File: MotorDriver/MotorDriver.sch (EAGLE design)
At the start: 52 parts, among them CN1 53375-0610, Q1 BUK7Y7R8-80EX, Q2 BUK7Y7R8-80EX, Q3 BUK7Y7R8-80EX, Q4 BUK7Y7R8-80EX, Q5 BUK7Y7R8-80EX, Q6 BUK7Y7R8-80EX, U1 LPC1549JBD48, U2 DRV8320SRTVT, U3 MCP1700T-33, U4 ADR5041

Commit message: SCT1_OUT[5, 6]を使うために配線を入れ替えた
1:    PWM_CL->MOSI
2:    PWM_CH->RX
22: RX->PWM_CH
33  MOSI->PWM_CL
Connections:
- net MOSI: now also U1.PIO0_0/ADC0_10/SCT0_OUT3; no longer U1.SWDIO/PIO0_20/SCT1_OUT6/TMS
- net PWM_CH: now also U1.PIO0_14/ADC1_7/SCT1_OUT5; no longer U1.PIO0_1/ADC0_7/SCT0_OUT4
- net PWM_CL: now also U1.SWDIO/PIO0_20/SCT1_OUT6/TMS; no longer U1.PIO0_0/ADC0_10/SCT0_OUT3
- net RX: now also U1.PIO0_1/ADC0_7/SCT0_OUT4; no longer U1.PIO0_14/ADC1_7/SCT1_OUT5
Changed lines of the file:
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@@
-</segment>
-</net>
-<net name="PWM_CH" class="0">
-<segment>
-<wire x1="10.16" y1="99.06" x2="-10.16" y2="99.06" width="0.1524" layer="91"/>
-<label x="-10.16" y="99.06" size="1.778" layer="95"/>
-<pinref part="U1" gate="G$1" pin="PIO0_1/ADC0_7/SCT0_OUT4"/>
-</segment>
-</net>
-<net name="PWM_CL" class="0">
-<segment>
-<wire x1="-10.16" y1="101.6" x2="10.16" y2="101.6" width="0.1524" layer="91"/>
-<label x="-10.16" y="101.6" size="1.778" layer="95"/>
-<pinref part="U1" gate="G$1" pin="PIO0_0/ADC0_10/SCT0_OUT3"/>
 </segment>
 </net>
@@
 <net name="RX" class="0">
 <segment>
-<pinref part="U1" gate="G$1" pin="PIO0_14/ADC1_7/SCT1_OUT5"/>
-<wire x1="60.96" y1="30.48" x2="60.96" y2="17.78" width="0.1524" layer="91"/>
-<label x="60.96" y="17.78" size="1.778" layer="95" rot="R90"/>
-</segment>
-<segment>
 <wire x1="203.2" y1="48.26" x2="187.96" y2="48.26" width="0.1524" layer="91"/>
 <label x="195.58" y="48.26" size="1.778" layer="95" rot="MR0"/>
 <pinref part="R27" gate="G$1" pin="1"/>
+</segment>
+<segment>
+<pinref part="U1" gate="G$1" pin="PIO0_1/ADC0_7/SCT0_OUT4"/>
+<wire x1="10.16" y1="99.06" x2="-10.16" y2="99.06" width="0.1524" layer="91"/>
+<label x="-10.16" y="99.06" size="1.778" layer="95"/>
 </segment>
 </net>
@@
 <net name="MOSI" class="0">
 <segment>
-<pinref part="U1" gate="G$1" pin="SWDIO/PIO0_20/SCT1_OUT6/TMS"/>
-<wire x1="93.98" y1="93.98" x2="109.22" y2="93.98" width="0.1524" layer="91"/>
-<label x="96.52" y="93.98" size="1.778" layer="95"/>
-</segment>
-<segment>
 <wire x1="137.16" y1="96.52" x2="124.46" y2="96.52" width="0.1524" layer="91"/>
 <label x="124.46" y="96.52" size="1.778" layer="95"/>
 <pinref part="CN1" gate="G$1" pin="4"/>
+</segment>
+<segment>
+<pinref part="U1" gate="G$1" pin="PIO0_0/ADC0_10/SCT0_OUT3"/>
+<wire x1="10.16" y1="101.6" x2="-10.16" y2="101.6" width="0.1524" layer="91"/>
+<label x="-10.16" y="101.6" size="1.778" layer="95"/>
 </segment>
 </net>
@@
 </segment>
 </net>
+<net name="PWM_CL" class="0">
+<segment>
+<pinref part="U1" gate="G$1" pin="SWDIO/PIO0_20/SCT1_OUT6/TMS"/>
+<wire x1="93.98" y1="93.98" x2="109.22" y2="93.98" width="0.1524" layer="91"/>
+<label x="96.52" y="93.98" size="1.778" layer="95"/>
+</segment>
+</net>
+<net name="PWM_CH" class="0">
+<segment>
+<pinref part="U1" gate="G$1" pin="PIO0_14/ADC1_7/SCT1_OUT5"/>
+<wire x1="60.96" y1="30.48" x2="60.96" y2="17.78" width="0.1524" layer="91"/>
+<label x="60.96" y="17.78" size="1.778" layer="95" rot="R90"/>
+</segment>
+</net>

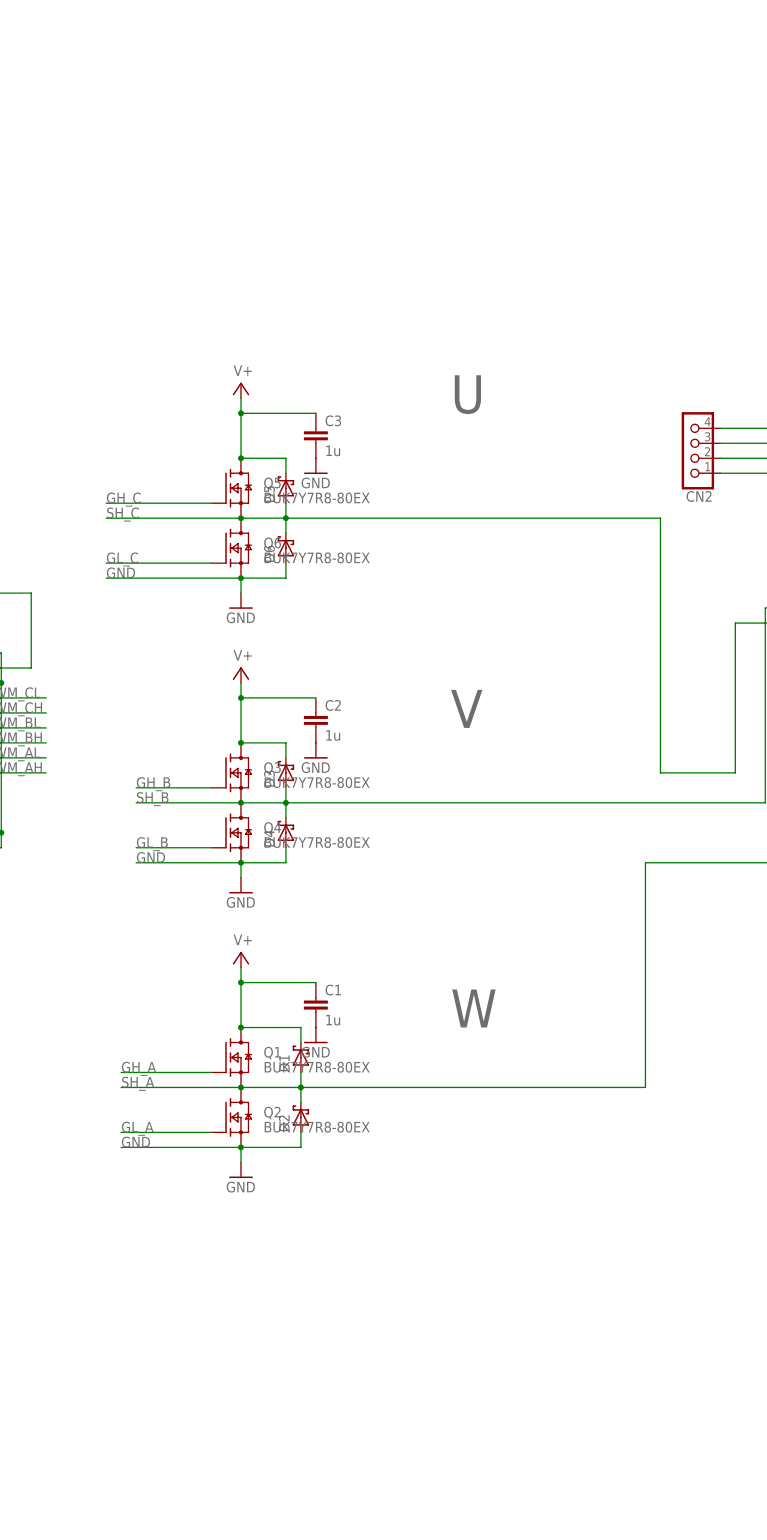
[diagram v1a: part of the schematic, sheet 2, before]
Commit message: FETのゲートソース間に抵抗を追加
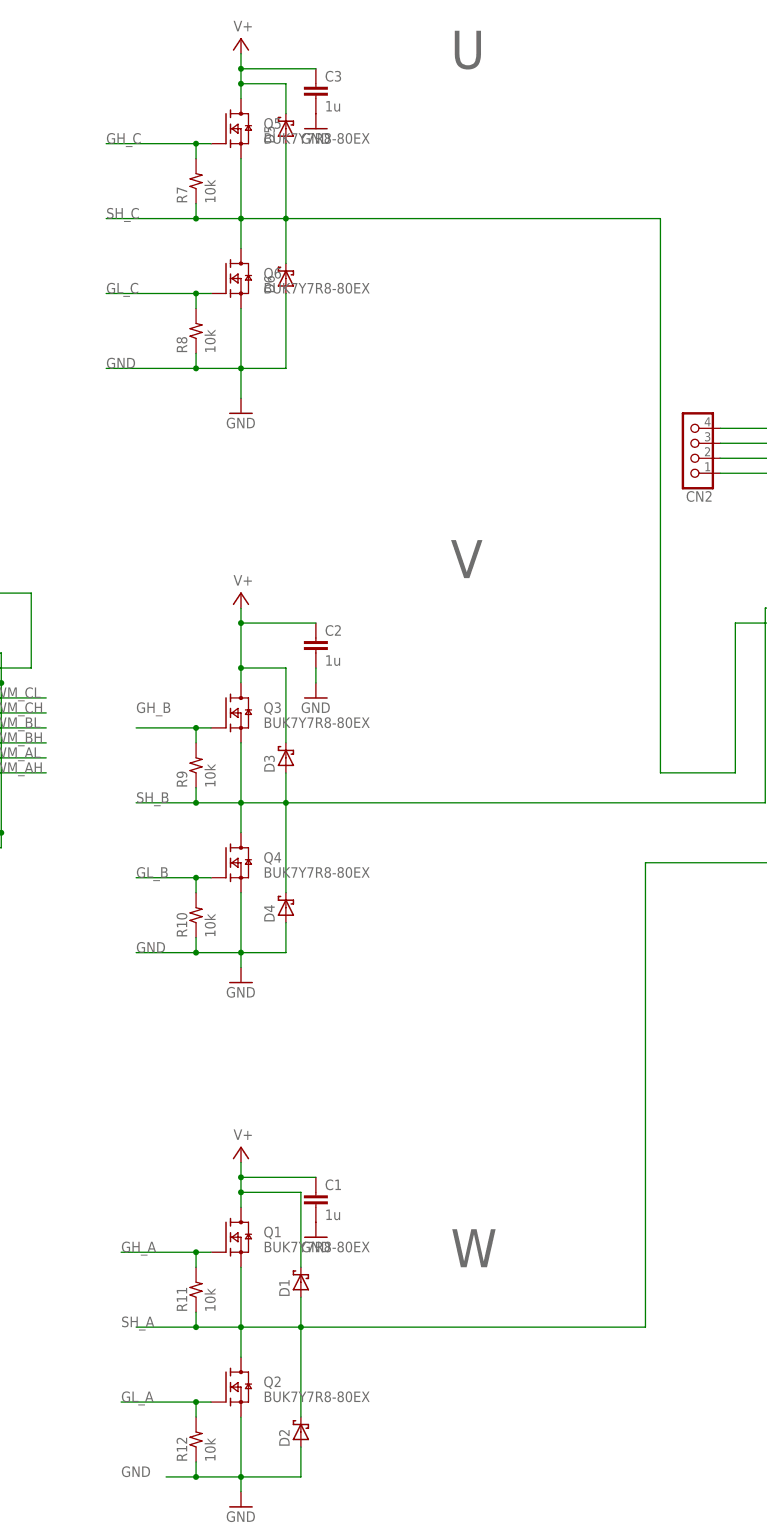
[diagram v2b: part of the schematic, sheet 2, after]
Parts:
- added R10, R11, R12, R7, R8, R9: 10k, Passive:R1608
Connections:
- net GH_A: now also R11.2
- net GH_B: now also R9.2
- net GH_C: now also R7.2
- net GL_A: now also R12.2
- net GL_B: now also R10.2
- net GL_C: now also R8.2
- net GND: now also R10.1, R12.1, R8.1
- net SH_A: now also R11.1
- net SH_B: now also R9.1
- net SH_C: now also R7.1
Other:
- moved on the sheet: C1, C2, C3, D1, D2, D3, D4, D5, D6, Q1, Q2, Q3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

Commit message: nya-n
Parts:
- C1, C10, C19, C2, C20, C3, C6, C9: device MotorDriver_Rev1:PASSIVE_C2012 -> MotorDriver:C2012
- C22, C23, C24: device Passive:C1608 -> MotorDriver:C1608
- C8: device MotorDriver_Rev1:PASSIVE_C1608 -> MotorDriver:C1608
- D7: device MotorDriver_Rev1:DIODE_SBD-SOD523 -> MotorDriver:SBD-SOD523
- LED0, LED1, LED2: device Opto:LED1608 -> MotorDriver:LED1608
- LED3: device Opto:LED1611R -> MotorDriver:LED1608
- R1, R10, R11, R12, R17, R2, R21, R23, R26, R27, R3, R32, R4, R5, R6, R7, R8, R9: device Passive:R1608 -> MotorDriver:R1608
- U1: device LPC1549JBD48:LPC1549JBD48 -> MotorDriver:LPC1549JBD48
- U2: device DRV8320SRTVT:DRV8320SRTVT -> MotorDriver:DRV8320SRTVT

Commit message: 機能追加 *CANバス *ホールセンサをダイレクトでDRVへ入力 *電源電圧監視 *DCDCをGDに内蔵 *15Aヒューズ
機能削減
*UART-DFUを廃止
*SPI接続を廃止
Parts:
- removed CN1: 53375-0610, MotorDriver:53375-0610
- removed CN4: (no value), nonolith.lbr:HEADER-1X3ROUND
- removed R10, R11, R12, R9: 10k, MotorDriver:R1608
- removed R26, R27: 100, MotorDriver:R1608
- removed U2: DRV8320SRTVT, MotorDriver:DRV8320SRTVT
- added C11: 10p, MotorDriver:C1005
- added C12: 10u, MotorDriver:C3225
- added C13: 100u, Passive:CPOLS-10
- added C4: 0.1u, MotorDriver:C1608
- added C5: 0.47u, MotorDriver:C1005
- added C7: 1u, MotorDriver:C1005
- added D10: SMAJ60A, MotorDriver:SBD-DO-214AC
- added D11: HSMS-2800-TR1G, HSMS-2800-TR1G:HSMS-2800-TR1G
- added D12: (no value), MotorDriver:SBD-SOD523
- added D8, D9: SDM2U40CSP-7B, SDM2U40CSP-7B:SDM2U40CSP-7B
- added F1: 15, Passive:F3216
- added IC1: DRV8320RSRHAR, DRV8320RSRHAR:DRV8320RSRHAR
- added IC2: MAX3051ESA+, MAX3051ESA+:MAX3051ESA+
- added J1: J_USB_MICROAB_HIROSE_ZX62-AB-5PA, j_usb_hirose_zx62-ab-5pa:J_USB_MICROAB_HIROSE_ZX62-AB-5PA
- added J2: SM03B-ZESS-TB, SM03B-ZESS-TB:SM03B-ZESS-TB
- added L1: NR5040T330M, NR5040T330M:NR5040T330M
- added R13, R14, R15, R16: 10, MotorDriver:R1608
- added R18: (no value), MotorDriver:R1005
- added R19, R24: 10k, MotorDriver:R1005
- added R20: 47k, MotorDriver:R1608
- added R22: 2.2k, MotorDriver:R1608
- added R25: 100k, MotorDriver:R1005
- added RF1: 900m, Passive:RF1608
- added Y1: FA238V, FA238V:FA238V
- C1, C2, C3, C6: value 1u -> 10u; device MotorDriver:C2012 -> MotorDriver:C3225
- C10: value 1u -> 10p; device MotorDriver:C2012 -> MotorDriver:C1005
- C19, C20: value 1u -> 0.1u; device MotorDriver:C2012 -> MotorDriver:C1005
- C22, C23, C24: device MotorDriver:C1608 -> MotorDriver:C1005
- C8: value 47n -> 1u; device MotorDriver:C1608 -> MotorDriver:C1005
- C9: value 1u -> 47n; device MotorDriver:C2012 -> MotorDriver:C1608
- D1, D2, D3, D4, D5, D6: value (none) -> NRVTSA4100ET3G
- D7: value (none) -> SDM2U40CSP-7B; device MotorDriver:SBD-SOD523 -> SDM2U40CSP-7B:SDM2U40CSP-7B
- R1: value 10k -> 12k; device MotorDriver:R1608 -> MotorDriver:R1005
- R17, R3: value 10k -> 10
- R2: value 10k -> 2.2k; device MotorDriver:R1608 -> MotorDriver:R1005
- R21, R23, R32, R4, R5, R6, R7, R8: device MotorDriver:R1608 -> MotorDriver:R1005
- SW1, SW2: device Switch:SKRP -> MotorDriver:SKRP
- U3: device ic-Microchip:MCP1700T-33 -> MotorDriver:MCP1700T-33
- U4: device ic-AD:ADR5041 -> MotorDriver:ADR5041
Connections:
- removed net !CS_DEV: CN1.2, U1.PIO0_24/SCTO_OUT6
- removed net MISO: CN1.3, U1.SWCLK/PIO0_19/TCK
- removed net MOSI: CN1.4, U1.PIO0_0/ADC0_10/SCT0_OUT3
- removed net PWM_AL: U1.PIO0_5/ADC0_3, U2.INLA
- removed net PWM_BH: U1.PIO0_3/ADC0_5/SCT1_OUT4, U2.INHB
- removed net PWM_BL: U1.PIO0_2/ADC0_6/SCT1_OUT3, U2.INLB
- removed net PWM_CH: U1.PIO0_14/ADC1_7/SCT1_OUT5, U2.INHC
- removed net PWM_CL: U1.SWDIO/PIO0_20/SCT1_OUT6/TMS, U2.INLC
- removed net RX: R27.1, U1.PIO0_1/ADC0_7/SCT0_OUT4
- removed net SCLK_DEV: CN1.5, U1.PIO0_17/WAKEUP/TRST
- removed net TX: R26.1, U1.PIO0_15/ADC1_8
- new net !BRAKE: IC1.INLC, U1.PIO0_27/ACMP_I1
- new net CANH: IC2.CANH, J2.2
- new net CANL: IC2.CANL, J2.3
- new net CAN_RX: IC2.RXD, U1.SWCLK/PIO0_19/TCK
- new net CAN_TX: IC2.TXD, U1.PIO0_17/WAKEUP/TRST
- new net D+: J1G$2.D+, U1.USB_DP
- new net D-: J1G$2.D-, U1.USB_DM
- new net DIR: IC1.INHC, U1.PIO0_28/ACMP1_I3
- new net ID: J1G$2.ID, R8.2, U1.PIO0_14/ADC1_7/SCT1_OUT5
- new net N$11: Q3.G, R14.2
- new net N$12: Q6.G, R13.2
- new net N$13: Q5.G, R3.2
- new net N$14: J1G$2.VB, RF1.1
- new net N$15: R18.2, U1.PIO0_16/ADC1_9
- new net N$16: C7.2, IC1.VCP
- new net N$17: C8.1, IC1.DVDD, R19.2, R24.2
- new net N$18: C9.1, IC1.CPL
- new net N$19: C9.2, IC1.CPH
- new net N$20: IC1.NSHDN, R25.2
- new net N$21: C11.1, U1.XTALOUT, Y1A.1
- new net N$22: C10.1, U1.XTALIN, Y1A.3
- new net N$23: U1.VBAT, U1.VDD(1)
- new net N$24: D12.A, J2.1
- new net N$26: CN5.P, F1.2
- new net N$4: C4.2, IC1.CB
- new net SHDN: IC2.SHDN, U1.PIO0_15/ADC1_8
- new net VBAT: C5.2, R20.1, R22.2, U1.PIO0_10/ADC1_2
- new net VBUS: D9.A, RF1.2, U1.PIO0_13/ADC1_6
- net !CS: now also IC1.NSCS, U1.PIO0_6/ADC0_2/SCT2_OUT3; no longer U1.PIO0_8/ADC0_O/TDO, U2.NSCS
- net !FAULT: now also IC1.NFAULT, R24.1, U1.PIO0_18/SCT0_OUT5; no longer R1.1, U2.NFAULT
- net !ISP: now also R7.1; no longer R17.1, U1.PIO0_16/ADC1_9
- net !RST: now also D12.K
- net +3V3: now also IC2.VCC, R18.1, R7.2; no longer R1.2, R17.2, R2.2, U1.VBAT, U1.VDD(1)
- net +5V: now also D8.K, D9.K; no longer CN1.1
- net GH_A: now also IC1.GHA, R16.1; no longer Q1.G, R11.2, U2.GHA
- net GH_B: now also IC1.GHB, R14.1; no longer Q3.G, R9.2, U2.GHB
- net GH_C: now also IC1.GHC, R3.1; no longer Q5.G, R7.2, U2.GHC
- net GL_A: now also IC1.GLA, R17.1; no longer Q2.G, R12.2, U2.GLA
- net GL_B: now also IC1.GLB, R15.1; no longer Q4.G, R10.2, U2.GLB
- net GL_C: now also IC1.GLC, R13.1; no longer Q6.G, R8.2, U2.GLC
- net GND: now also C10.2, C11.2, C12.2, C13.N, C5.1, C8.2, CN3.6, D10.A, D11.ANODE, IC1.AGND, IC1.BGND, IC1.GND, IC1.PGND, IC1.SLA, IC1.SLB, IC1.SLC, IC1.THERMAL_PAD, IC2.GND, IC2.RS, J1G$1.S1, J1G$1.S2, J1G$1.S3, J1G$1.S4, J1G$2.GND, R2.2, R22.1, Y1B.1; no longer C9.2, CN1.6, CN3.5, CN4.1, R10.1, R12.1, R3.1, U2.AGND, U2.PGND, U2.SLA, U2.SLB, U2.SLC, U2.THERMAL_PAD
- net HALL_U: now also IC1.INLA, U1.PIO0_1/ADC0_7/SCT0_OUT4; no longer U1.PIO0_27/ACMP_I1
- net HALL_V: now also IC1.INHB, U1.PIO0_0/ADC0_10/SCT0_OUT3; no longer U1.PIO0_26/ACMP0_13/SCT3_OUT3
- net HALL_W: now also IC1.INLB, U1.PIO0_29/ACMP2_I3/SCT2_OUT4; no longer U1.PIO0_25/ACMP0_14
- net LED0: now also U1.PIO0_3/ADC0_5/SCT1_OUT4; no longer U1.PIO0_11/ADC1_3
- net LED1: now also U1.PIO0_26/ACMP0_13/SCT3_OUT3; no longer U1.PIO0_12/DAC_OUT
- net LED2: now also U1.PIO0_25/ACMP0_14; no longer U1.PIO0_13/ADC1_6
- net N$1: now also IC1.FB, R1.2, R2.1; no longer CN4.2, R26.2
- net N$2: now also D8.A, L1.1, R1.1; no longer CN4.3, R27.2
- net N$3: now also C4.1, D11.CATHODE, IC1.SW, L1.2; no longer C10.1, U2.VCP
- net N$5: now also Q2.G, R17.2; no longer C8.1, U2.CPH
- net N$6: now also Q1.G, R16.2; no longer C8.2, U2.CPL
- net N$7: now also Q4.G, R15.2; no longer C9.1, U2.DVDD
- net PWM_AH: now also IC1.INHA, U1.PIO0_2/ADC0_6/SCT1_OUT3; no longer U1.PIO0_6/ADC0_2/SCT2_OUT3, U2.INHA
- net PWM_EN: now also IC1.ENABLE, U1.PIO0_5/ADC0_3; no longer R3.2, U1.PIO0_7/ADC0_1, U2.ENABLE
- net QEI_A: now also U1.PIO0_11/ADC1_3; no longer U1.PIO0_28/ACMP1_I3
- net QEI_B: now also U1.PIO0_12/DAC_OUT; no longer U1.PIO0_29/ACMP2_I3/SCT2_OUT4
- net SCLK: now also IC1.SCLK, U1.PIO0_7/ADC0_1; no longer U1.PIO0_9/ADC1_1/TDI, U2.SCLK
- net SDI: now also IC1.SDI, U1.PIO0_8/ADC0_O/TDO; no longer U1.PIO0_18/SCT0_OUT5, U2.SDI
- net SDO: now also IC1.SDO, R19.1, U1.PIO0_9/ADC1_1/TDI; no longer R2.1, U1.PIO0_10/ADC1_2, U2.SDO
- net SH_A: now also IC1.SHA; no longer R11.1, U2.SHA
- net SH_B: now also IC1.SHB; no longer R9.1, U2.SHB
- net SH_C: now also CN3.5, IC1.SHC; no longer CN3.6, R7.1, U2.SHC
- net V+: now also C12.1, C13.P, C7.1, D10.K, F1.1, IC1.VDRAIN, IC1.VIN, IC1.VM, R20.2, R25.1; no longer C10.2, CN5.P, U2.VDRAIN, U2.VM
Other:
- note added: "16[V]"
- note added: "3413.0330.22"
- note added: "6.3[V]"
- note added: "63[V]"
- note added: "GRM32EC72A106KE05L"
- note added: "SBDの記号だけどツェナー"
